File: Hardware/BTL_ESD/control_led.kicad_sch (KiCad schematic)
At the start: 10 parts, among them J6 220VAC, K1 SRD-05VDC-SL-C, Q4 MMBT2222A, U9 PC817

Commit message: update
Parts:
- removed C58: 10uF/16V, Capacitor_SMD:C_0603_1608Metric_Pad1.08x0.95mm_HandSolder, symbol Device:C_Small
- removed C59: 100nF/16V, Capacitor_SMD:C_0603_1608Metric_Pad1.08x0.95mm_HandSolder, symbol Device:C_Small
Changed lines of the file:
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@@
   (junction (at 139.7 100.33) (diameter 0) (color 0 0 0 0)
   )
-  (junction (at 139.7 154.94) (diameter 0) (color 0 0 0 0)
-  )
   (junction (at 139.7 83.82) (diameter 0) (color 0 0 0 0)
-  )
-  (junction (at 139.7 147.32) (diameter 0) (color 0 0 0 0)
   )
   (no_connect (at 161.29 97.79))
@@
     (stroke (width 0) (type default))
   )
-  (wire (pts (xy 147.32 153.67) (xy 147.32 154.94))
-    (stroke (width 0) (type default))
-  )
   (wire (pts (xy 134.62 87.63) (xy 134.62 90.17))
     (stroke (width 0) (type default))
@@
     (stroke (width 0) (type default))
   )
-  (wire (pts (xy 147.32 154.94) (xy 139.7 154.94))
-    (stroke (width 0) (type default))
-  )
-  (wire (pts (xy 139.7 154.94) (xy 132.08 154.94))
-    (stroke (width 0) (type default))
-  )
   (wire (pts (xy 161.29 92.71) (xy 171.45 92.71))
     (stroke (width 0) (type default))
   )
-  (wire (pts (xy 139.7 144.78) (xy 139.7 147.32))
-    (stroke (width 0) (type default))
-  )
-  (wire (pts (xy 132.08 154.94) (xy 132.08 153.67))
-    (stroke (width 0) (type default))
-  )
   (wire (pts (xy 171.45 92.71) (xy 171.45 104.14))
     (stroke (width 0) (type default))
@@
     (stroke (width 0) (type default))
   )
-  (wire (pts (xy 139.7 147.32) (xy 132.08 147.32))
-    (stroke (width 0) (type default))
-  )
   (wire (pts (xy 146.05 97.79) (xy 146.05 100.33))
     (stroke (width 0) (type default))
@@
     (stroke (width 0) (type default))
   )
-  (wire (pts (xy 147.32 147.32) (xy 147.32 148.59))
-    (stroke (width 0) (type default))
-  )
   (wire (pts (xy 171.45 104.14) (xy 182.88 104.14))
     (stroke (width 0) (type default))
@@
     (stroke (width 0) (type default))
   )
-  (wire (pts (xy 139.7 147.32) (xy 147.32 147.32))
-    (stroke (width 0) (type default))
-  )
   (wire (pts (xy 139.7 83.82) (xy 139.7 87.63))
     (stroke (width 0) (type default))
@@
     (stroke (width 0) (type default))
   )
-  (wire (pts (xy 139.7 154.94) (xy 139.7 157.48))
-    (stroke (width 0) (type default))
-  )
   (wire (pts (xy 209.55 92.71) (xy 207.01 92.71))
     (stroke (width 0) (type default))
@@
   )
   (wire (pts (xy 139.7 87.63) (xy 146.05 87.63))
-    (stroke (width 0) (type default))
-  )
-  (wire (pts (xy 132.08 148.59) (xy 132.08 147.32))
     (stroke (width 0) (type default))
   )
@@
     )
   )
-  (symbol (lib_id "power:GND") (at 139.7 157.48 0) (unit 1)
-    (in_bom yes) (on_board yes) (dnp no) (fields_autoplaced)
-    (property "Reference" "#PWR081" (at 139.7 163.83 0)
-      (effects (font (size 1.27 1.27)) hide)
-    )
-    (property "Value" "GND" (at 139.7 162.56 0)
-      (effects (font (size 1.27 1.27)))
-    )
-    (property "Footprint" "" (at 139.7 157.48 0)
-      (effects (font (size 1.27 1.27)) hide)
-    )
-    (property "Datasheet" "" (at 139.7 157.48 0)
-      (effects (font (size 1.27 1.27)) hide)
-    )
-    (pin "1")
-    (instances
-      (project "BTL_ESD"
-        (path "/ce4779b4-6d78-42e3-84df-0a4e77629b0f/aa65e15e-8b54-480e-8def-56214b53193f"
-          (reference "#PWR081") (unit 1)
-        )
-      )
-    )
-  )
   (symbol (lib_id "power:+3V3") (at 86.36 102.87 0) (unit 1)
     (in_bom yes) (on_board yes) (dnp no) (fields_autoplaced)
@@
         )
       )
-    )
-  )
-  (symbol (lib_id "Device:C_Small") (at 132.08 151.13 0) (unit 1)
-    (in_bom yes) (on_board yes) (dnp no) (fields_autoplaced)
-    (property "Reference" "C58" (at 134.62 149.8663 0)
-      (effects (font (size 1.27 1.27)) (justify left))
-    )
-    (property "Value" "10uF/16V" (at 134.62 152.4063 0)
-      (effects (font (size 1.27 1.27)) (justify left))
-    )
-    (property "Footprint" "Capacitor_SMD:C_0603_1608Metric_Pad1.08x0.95mm_HandSolder" (at 132.08 151.13 0)
-      (effects (font (size 1.27 1.27)) hide)
-    )
-    (property "Datasheet" "~" (at 132.08 151.13 0)
-      (effects (font (size 1.27 1.27)) hide)
-    )
-    (property "URL" "https://www.thegioiic.com/tu-gom-0603-10uf-16v" (at 132.08 151.13 0)
-      (effects (font (size 1.27 1.27)) hide)
-    )
-    (pin "1")
-    (pin "2")
-    (instances
-      (project "BTL_ESD"
-        (path "/ce4779b4-6d78-42e3-84df-0a4e77629b0f/aa65e15e-8b54-480e-8def-56214b53193f"
-          (reference "C58") (unit 1)
-        )
-      )
-    )
-  )
-  (symbol (lib_id "power:+3V3") (at 139.7 144.78 0) (unit 1)
-    (in_bom yes) (on_board yes) (dnp no) (fields_autoplaced)
-    (property "Reference" "#PWR080" (at 139.7 148.59 0)
-      (effects (font (size 1.27 1.27)) hide)
-    )
-    (property "Value" "+3V3" (at 139.7 139.7 0)
-      (effects (font (size 1.27 1.27)))
-    )
-    (property "Footprint" "" (at 139.7 144.78 0)
-      (effects (font (size 1.27 1.27)) hide)
-    )
-    (property "Datasheet" "" (at 139.7 144.78 0)
-      (effects (font (size 1.27 1.27)) hide)
-    )
-    (pin "1")
-    (instances
-      (project "BTL_ESD"
-        (path "/ce4779b4-6d78-42e3-84df-0a4e77629b0f/aa65e15e-8b54-480e-8def-56214b53193f"
-          (reference "#PWR080") (unit 1)
-        )
-      )
-    )
-  )
-  (symbol (lib_id "Device:C_Small") (at 147.32 151.13 0) (unit 1)
-    (in_bom yes) (on_board yes) (dnp no) (fields_autoplaced)
-    (property "Reference" "C59" (at 149.86 149.8663 0)
-      (effects (font (size 1.27 1.27)) (justify left))
-    )
-    (property "Value" "100nF/16V" (at 149.86 152.4063 0)
-      (effects (font (size 1.27 1.27)) (justify left))
-    )
-    (property "Footprint" "Capacitor_SMD:C_0603_1608Metric_Pad1.08x0.95mm_HandSolder" (at 147.32 151.13 0)
-      (effects (font (size 1.27 1.27)) hide)
-    )
-    (property "Datasheet" "~" (at 147.32 151.13 0)
-      (effects (font (size 1.27 1.27)) hide)
-    )
-    (property "URL" "https://www.thegioiic.com/tu-gom-0603-100nf-0-1uf-16v" (at 147.32 151.13 0)
-      (effects (font (size 1.27 1.27)) hide)
-    )
-    (pin "2")
-    (pin "1")
-    (instances
-      (project "BTL_ESD"
-        (path "/ce4779b4-6d78-42e3-84df-0a4e77629b0f/aa65e15e-8b54-480e-8def-56214b53193f"
-          (reference "C59") (unit 1)
-        )
-      )

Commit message: update
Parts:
- RV1: value 665V -> 470V; footprint Varistor:RV_Disc_D21.5mm_W4.3mm_P10mm -> Varistor:RV_Disc_D12mm_W3.9mm_P7.5mm; URL https://www.thegioiic.com/tu-chong-set-varistor-420l40-665v -> https://www.thegioiic.com/tu-chong-set-varistor-14d471k-470v
- renumbered D10 to D11, R29 to R30, R30 to R31
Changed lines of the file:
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@@
   (symbol (lib_id "SS34:SS34") (at 134.62 93.98 90) (unit 1)
     (in_bom yes) (on_board yes) (dnp no) (fields_autoplaced)
-    (property "Reference" "D10" (at 137.16 92.3925 90)
+    (property "Reference" "D11" (at 137.16 92.3925 90)
       (effects (font (size 1.27 1.27)) (justify right))
     )
@@
       (project "BTL_ESD"
         (path "/ce4779b4-6d78-42e3-84df-0a4e77629b0f/aa65e15e-8b54-480e-8def-56214b53193f"
-          (reference "D10") (unit 1)
+          (reference "D11") (unit 1)
         )
       )
@@
   (symbol (lib_id "power:+5V") (at 139.7 82.55 0) (unit 1)
     (in_bom yes) (on_board yes) (dnp no) (fields_autoplaced)
-    (property "Reference" "#PWR078" (at 139.7 86.36 0)
+    (property "Reference" "#PWR081" (at 139.7 86.36 0)
       (effects (font (size 1.27 1.27)) hide)
     )
@@
       (project "BTL_ESD"
         (path "/ce4779b4-6d78-42e3-84df-0a4e77629b0f/aa65e15e-8b54-480e-8def-56214b53193f"
-          (reference "#PWR078") (unit 1)
+          (reference "#PWR081") (unit 1)
         )
       )
@@
   (symbol (lib_id "power:GND") (at 139.7 121.92 0) (unit 1)
     (in_bom yes) (on_board yes) (dnp no) (fields_autoplaced)
-    (property "Reference" "#PWR079" (at 139.7 128.27 0)
+    (property "Reference" "#PWR082" (at 139.7 128.27 0)
       (effects (font (size 1.27 1.27)) hide)
     )
@@
       (project "BTL_ESD"
         (path "/ce4779b4-6d78-42e3-84df-0a4e77629b0f/aa65e15e-8b54-480e-8def-56214b53193f"
-          (reference "#PWR079") (unit 1)
+          (reference "#PWR082") (unit 1)
         )
       )
@@
       (effects (font (size 1.27 1.27)) (justify left))
     )
-    (property "Value" "665V" (at 185.42 98.0468 0)
+    (property "Value" "470V" (at 185.42 98.0468 0)
       (effects (font (size 1.27 1.27)) (justify left))
     )
-    (property "Footprint" "Varistor:RV_Disc_D21.5mm_W4.3mm_P10mm" (at 181.102 96.52 90)
+    (property "Footprint" "Varistor:RV_Disc_D12mm_W3.9mm_P7.5mm" (at 181.102 96.52 90)
       (effects (font (size 1.27 1.27)) hide)
     )
@@
       (effects (font (size 1.27 1.27)) hide)
     )
-    (property "URL" "https://www.thegioiic.com/tu-chong-set-varistor-420l40-665v" (at 182.88 96.52 0)
+    (property "URL" "https://www.thegioiic.com/tu-chong-set-varistor-14d471k-470v" (at 182.88 96.52 0)
       (effects (font (size 1.27 1.27)) hide)
     )
@@
   (symbol (lib_id "Device:R_US") (at 125.73 110.49 90) (unit 1)
     (in_bom yes) (on_board yes) (dnp no) (fields_autoplaced)
-    (property "Reference" "R30" (at 125.73 104.14 90)
+    (property "Reference" "R31" (at 125.73 104.14 90)
       (effects (font (size 1.27 1.27)))
     )
@@
       (project "BTL_ESD"
         (path "/ce4779b4-6d78-42e3-84df-0a4e77629b0f/aa65e15e-8b54-480e-8def-56214b53193f"
-          (reference "R30") (unit 1)
+          (reference "R31") (unit 1)
         )
       )
@@
   (symbol (lib_id "Device:R_Small_US") (at 93.98 105.41 90) (unit 1)
     (in_bom yes) (on_board yes) (dnp no) (fields_autoplaced)
-    (property "Reference" "R29" (at 93.98 99.06 90)
+    (property "Reference" "R30" (at 93.98 99.06 90)
       (effects (font (size 1.27 1.27)))
     )
@@
       (project "BTL_ESD"
         (path "/ce4779b4-6d78-42e3-84df-0a4e77629b0f/aa65e15e-8b54-480e-8def-56214b53193f"
-          (reference "R29") (unit 1)
+          (reference "R30") (unit 1)
         )
       )
@@
   (symbol (lib_id "power:+3V3") (at 86.36 102.87 0) (unit 1)
     (in_bom yes) (on_board yes) (dnp no) (fields_autoplaced)
-    (property "Reference" "#PWR077" (at 86.36 106.68 0)
+    (property "Reference" "#PWR080" (at 86.36 106.68 0)
       (effects (font (size 1.27 1.27)) hide)
     )
@@
       (project "BTL_ESD"
         (path "/ce4779b4-6d78-42e3-84df-0a4e77629b0f/aa65e15e-8b54-480e-8def-56214b53193f"
-          (reference "#PWR077") (unit 1)
-        )
-      )
+          (reference "#PWR080") (unit 1)
+        )
+      )

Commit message: fea:STM32: upload structure fodler
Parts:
- renumbered J6 to J7, R30 to R31, R31 to R32
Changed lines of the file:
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@@
   (symbol (lib_id "Device:R_US") (at 125.73 110.49 90) (unit 1)
     (in_bom yes) (on_board yes) (dnp no) (fields_autoplaced)
-    (property "Reference" "R31" (at 125.73 104.14 90)
+    (property "Reference" "R32" (at 125.73 104.14 90)
       (effects (font (size 1.27 1.27)))
     )
@@
       (project "BTL_ESD"
         (path "/ce4779b4-6d78-42e3-84df-0a4e77629b0f/aa65e15e-8b54-480e-8def-56214b53193f"
-          (reference "R31") (unit 1)
+          (reference "R32") (unit 1)
         )
       )
@@
   (symbol (lib_id "Device:R_Small_US") (at 93.98 105.41 90) (unit 1)
     (in_bom yes) (on_board yes) (dnp no) (fields_autoplaced)
-    (property "Reference" "R30" (at 93.98 99.06 90)
+    (property "Reference" "R31" (at 93.98 99.06 90)
       (effects (font (size 1.27 1.27)))
     )
@@
       (project "BTL_ESD"
         (path "/ce4779b4-6d78-42e3-84df-0a4e77629b0f/aa65e15e-8b54-480e-8def-56214b53193f"
-          (reference "R30") (unit 1)
+          (reference "R31") (unit 1)
         )
       )
@@
   (symbol (lib_id "Connector:Conn_01x04_Socket") (at 214.63 92.71 0) (unit 1)
     (in_bom yes) (on_board yes) (dnp no) (fields_autoplaced)
-    (property "Reference" "J6" (at 215.9 92.71 0)
+    (property "Reference" "J7" (at 215.9 92.71 0)
       (effects (font (size 1.27 1.27)) (justify left))
     )
@@
       (project "BTL_ESD"
         (path "/ce4779b4-6d78-42e3-84df-0a4e77629b0f/aa65e15e-8b54-480e-8def-56214b53193f"
-          (reference "J6") (unit 1)
+          (reference "J7") (unit 1)
         )
       )

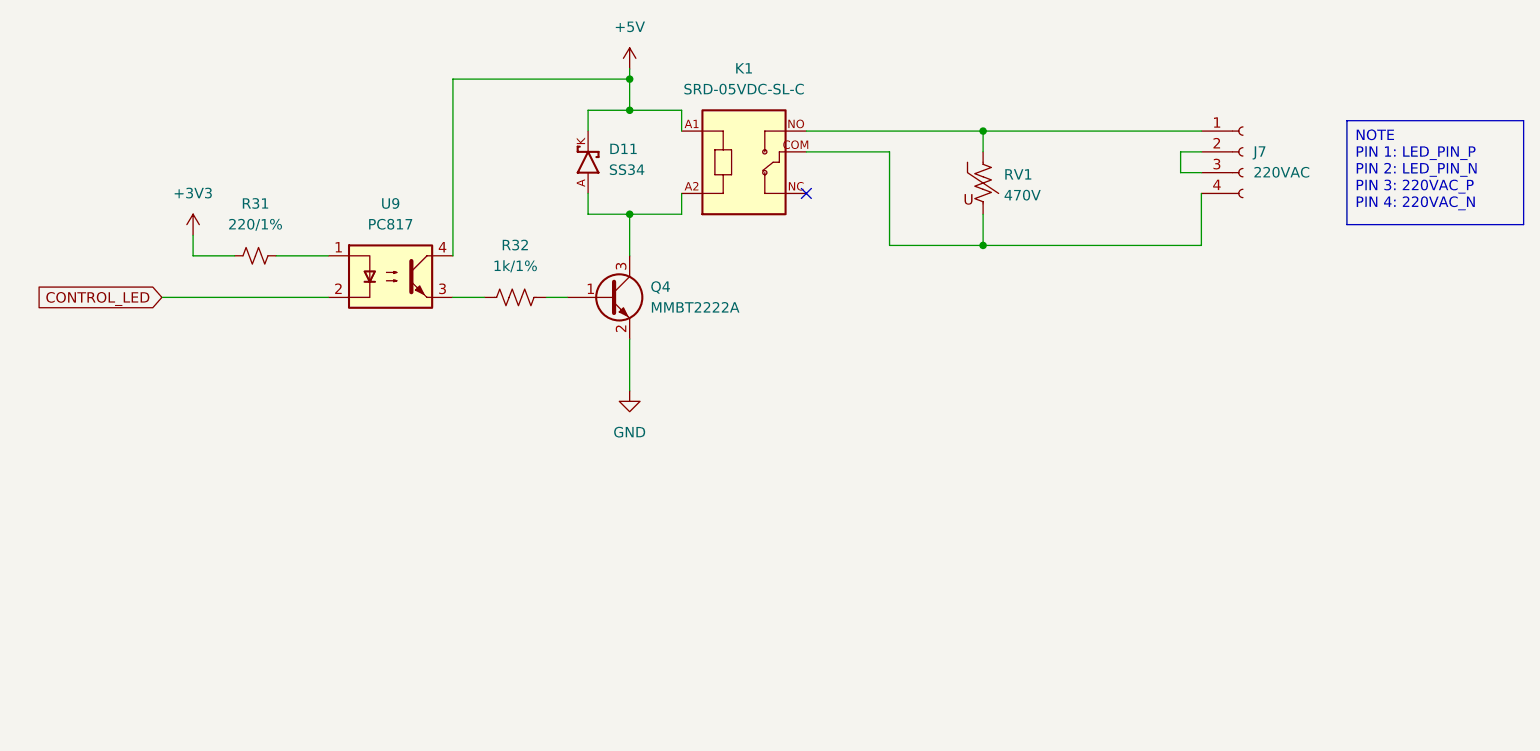
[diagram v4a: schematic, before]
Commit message: code:ESP32: update uart driver, main.c && hardware file pcb
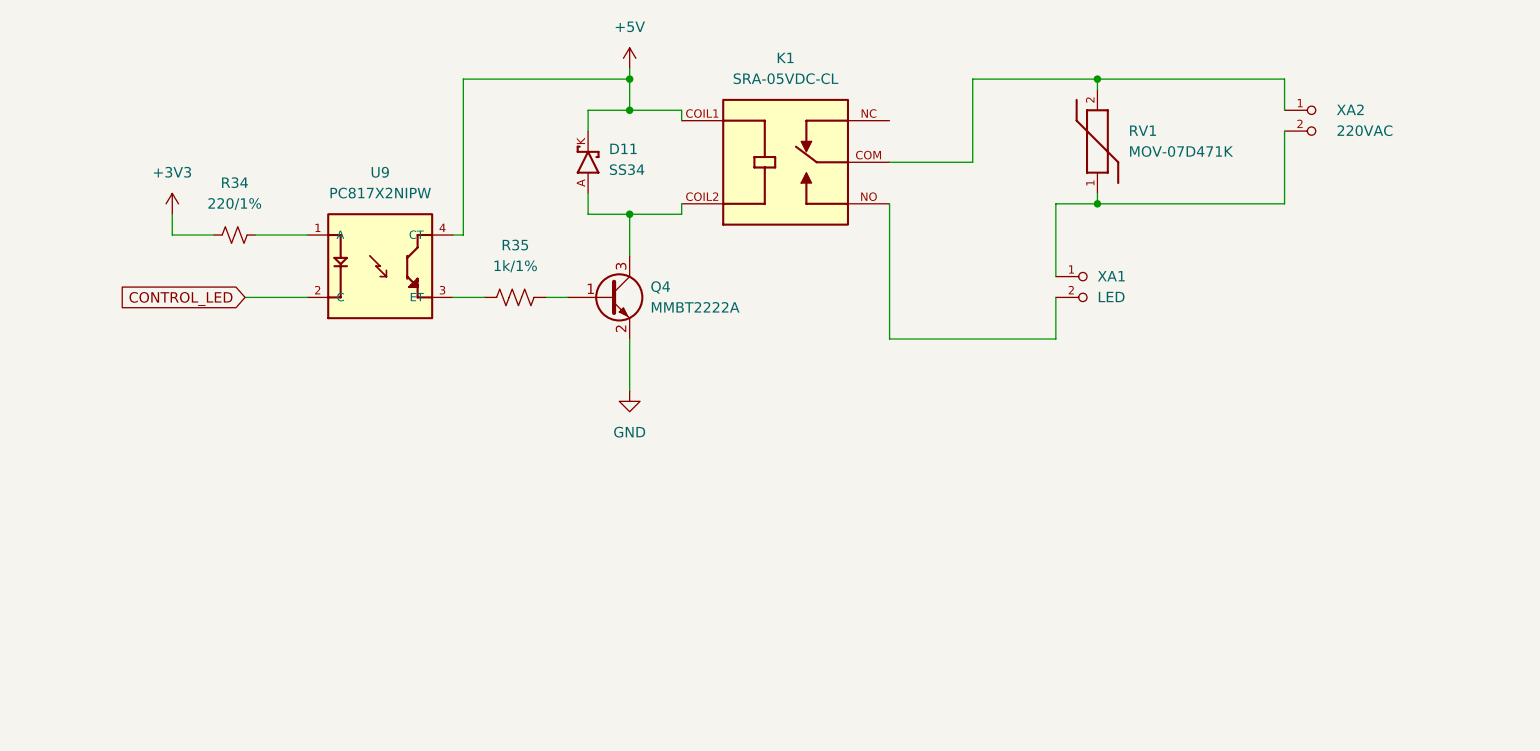
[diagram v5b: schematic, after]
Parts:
- removed J7: 220VAC, HB9500:HB9500_9_5_4P, symbol Connector:Conn_01x04_Socket
- removed K1: SRD-05VDC-SL-C, SRD-05VDC-SL-C:RELAY_SRD-05VDC-SL-C, symbol SRD-05VDC-SL-C:SRD-05VDC-SL-C
- removed RV1: 470V, Varistor:RV_Disc_D12mm_W3.9mm_P7.5mm, symbol Device:Varistor_US
- removed U9: PC817, Package_DIP:DIP-4_W7.62mm, symbol Isolator:PC817
- added K1: SRA-05VDC-CL, SRA-05VDC-CL:RELAY_SRA-05VDC-CL, symbol SRA-05VDC-CL:SRA-05VDC-CL
- added RV1: MOV-07D471K, MOV-14D471K:MOV07D471K, symbol MOV-14D471K:MOV-07D471K
- added U9: PC817X2NIPW, PC817X2NIP0F:SOT254P975X400-4N, symbol PC817X2NIP0F:PC817X2NIP0F
- added XA1: LED, MKDS1_2-3:PHOENIX_MKDS1_2-3.81, symbol MKDS1_2-3.81:MKDS1_2-3.81
- added XA2: 220VAC, MKDS1_2-3:PHOENIX_MKDS1_2-3.81, symbol MKDS1_2-3.81:MKDS1_2-3.81
- renumbered R31 to R34, R32 to R35
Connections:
- net +5V: now also K1.COIL1, U9.4 (CT)
- net CONTROL_LED: now also U9.2 (C)
- net at D11.A, Q4.3: now also K1.COIL2
- net at R34.2: now also U9.1 (A)
- net at R35.1: now also U9.3 (ET)
- new net: K1.COM, RV1.2, XA2.1
- new net: K1.NO, XA1.2
- new net: RV1.1, XA1.1, XA2.2
- no-connect marks 1 -> 0
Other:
- moved on the sheet: R34
